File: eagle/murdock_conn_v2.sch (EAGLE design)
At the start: 12 parts, among them X1 GPS, X2 IMU, X7 MURDOCK_STACK

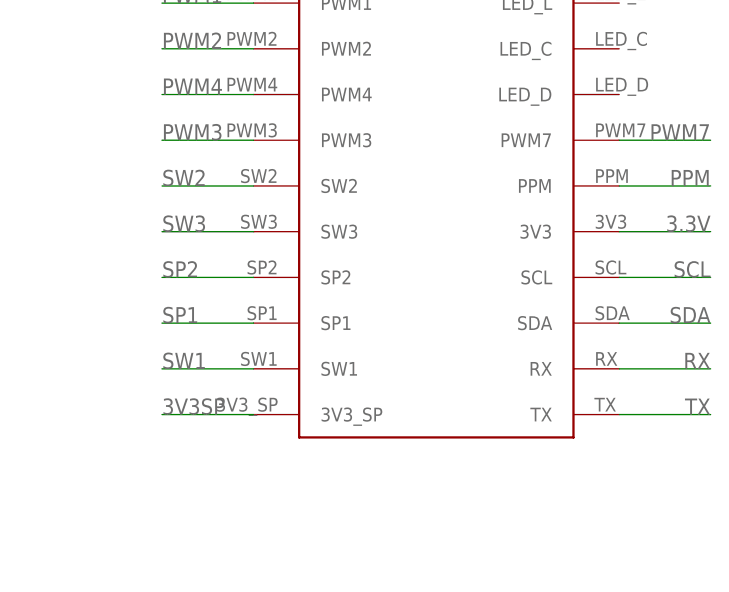
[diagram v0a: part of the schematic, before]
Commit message: updated stack schematic
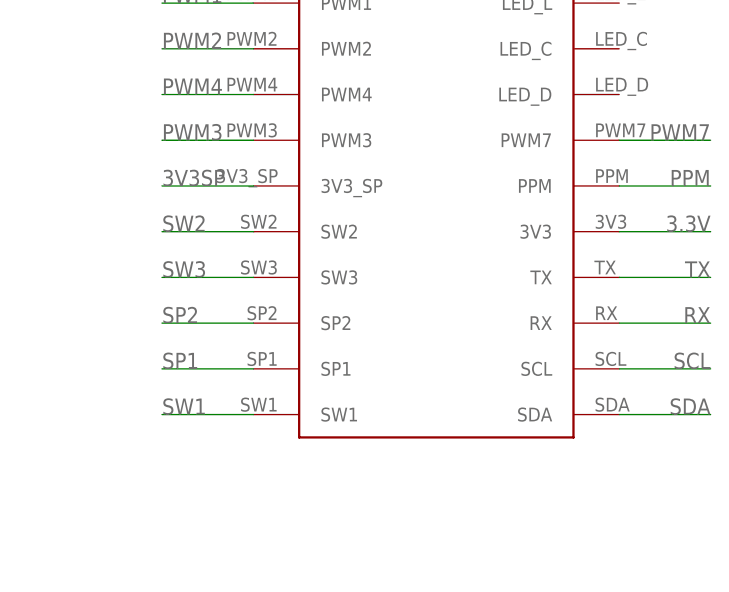
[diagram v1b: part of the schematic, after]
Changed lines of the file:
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@@
 <?xml version="1.0" encoding="utf-8"?>
 <!DOCTYPE eagle SYSTEM "eagle.dtd">
-<eagle version="6.2">
+<eagle version="6.4">
 <drawing>
 <settings>
@@
 <segment>
 <pinref part="X7" gate="G$1" pin="SDA"/>
-<wire x1="167.64" y1="43.18" x2="177.8" y2="43.18" width="0.1524" layer="91"/>
-<label x="177.8" y="43.18" size="1.778" layer="95" rot="MR0"/>
+<wire x1="167.64" y1="33.02" x2="177.8" y2="33.02" width="0.1524" layer="91"/>
+<label x="177.8" y="33.02" size="1.778" layer="95" rot="MR0"/>
 </segment>
 </net>
@@
 <segment>
 <pinref part="X7" gate="G$1" pin="SCL"/>
-<wire x1="167.64" y1="48.26" x2="177.8" y2="48.26" width="0.1524" layer="91"/>
-<label x="177.8" y="48.26" size="1.778" layer="95" rot="MR0"/>
+<wire x1="167.64" y1="38.1" x2="177.8" y2="38.1" width="0.1524" layer="91"/>
+<label x="177.8" y="38.1" size="1.778" layer="95" rot="MR0"/>
 </segment>
 </net>
@@
 <segment>
 <pinref part="X7" gate="G$1" pin="RX"/>
-<wire x1="167.64" y1="38.1" x2="177.8" y2="38.1" width="0.1524" layer="91"/>
-<label x="177.8" y="38.1" size="1.778" layer="95" rot="MR0"/>
+<wire x1="167.64" y1="43.18" x2="177.8" y2="43.18" width="0.1524" layer="91"/>
+<label x="177.8" y="43.18" size="1.778" layer="95" rot="MR0"/>
 </segment>
 </net>
@@
 <segment>
 <pinref part="X7" gate="G$1" pin="TX"/>
-<wire x1="167.64" y1="33.02" x2="177.8" y2="33.02" width="0.1524" layer="91"/>
-<label x="177.8" y="33.02" size="1.778" layer="95" rot="MR0"/>
+<wire x1="167.64" y1="48.26" x2="177.8" y2="48.26" width="0.1524" layer="91"/>
+<label x="177.8" y="48.26" size="1.778" layer="95" rot="MR0"/>
 </segment>
 </net>
@@
 <segment>
 <pinref part="X7" gate="G$1" pin="3V3_SP"/>
-<wire x1="127" y1="33.02" x2="116.84" y2="33.02" width="0.1524" layer="91"/>
-<label x="116.84" y="33.02" size="1.778" layer="95"/>
+<wire x1="127" y1="58.42" x2="116.84" y2="58.42" width="0.1524" layer="91"/>
+<label x="116.84" y="58.42" size="1.778" layer="95"/>
 </segment>
 </net>
@@
 <segment>
 <pinref part="X7" gate="G$1" pin="SP1"/>
-<wire x1="127" y1="43.18" x2="116.84" y2="43.18" width="0.1524" layer="91"/>
-<label x="116.84" y="43.18" size="1.778" layer="95"/>
+<wire x1="127" y1="38.1" x2="116.84" y2="38.1" width="0.1524" layer="91"/>
+<label x="116.84" y="38.1" size="1.778" layer="95"/>
 </segment>
 </net>
@@
 <segment>
 <pinref part="X7" gate="G$1" pin="SP2"/>
-<wire x1="127" y1="48.26" x2="116.84" y2="48.26" width="0.1524" layer="91"/>
-<label x="116.84" y="48.26" size="1.778" layer="95"/>
+<wire x1="127" y1="43.18" x2="116.84" y2="43.18" width="0.1524" layer="91"/>
+<label x="116.84" y="43.18" size="1.778" layer="95"/>
 </segment>
 </net>
@@
 <segment>
 <pinref part="X7" gate="G$1" pin="SW3"/>
-<wire x1="127" y1="53.34" x2="116.84" y2="53.34" width="0.1524" layer="91"/>
-<label x="116.84" y="53.34" size="1.778" layer="95"/>
+<wire x1="127" y1="48.26" x2="116.84" y2="48.26" width="0.1524" layer="91"/>
+<label x="116.84" y="48.26" size="1.778" layer="95"/>
 </segment>
 </net>
@@
 <segment>
 <pinref part="X7" gate="G$1" pin="SW2"/>
-<wire x1="127" y1="58.42" x2="116.84" y2="58.42" width="0.1524" layer="91"/>
-<label x="116.84" y="58.42" size="1.778" layer="95"/>
+<wire x1="127" y1="53.34" x2="116.84" y2="53.34" width="0.1524" layer="91"/>
+<label x="116.84" y="53.34" size="1.778" layer="95"/>
 </segment>
 </net>
@@
 <segment>
 <pinref part="X7" gate="G$1" pin="SW1"/>
-<wire x1="127" y1="38.1" x2="116.84" y2="38.1" width="0.1524" layer="91"/>
-<label x="116.84" y="38.1" size="1.778" layer="95"/>
-</segment>
-</net>
+<wire x1="127" y1="33.02" x2="116.84" y2="33.02" width="0.1524" layer="91"/>
+<label x="116.84" y="33.02" size="1.778" layer="95"/>
+</segment>
+</net>
